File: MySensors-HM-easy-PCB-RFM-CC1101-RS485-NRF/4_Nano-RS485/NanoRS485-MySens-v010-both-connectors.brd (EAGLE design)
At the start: 25 x 35.5 mm, 47 parts, among them IC1 ATSHA204A, IC2 AT25DF512C-SSHN-B, IC3 REG1117, IC31 ATMEGA168-TQFP, X2 1751264, Y2 8MHZ

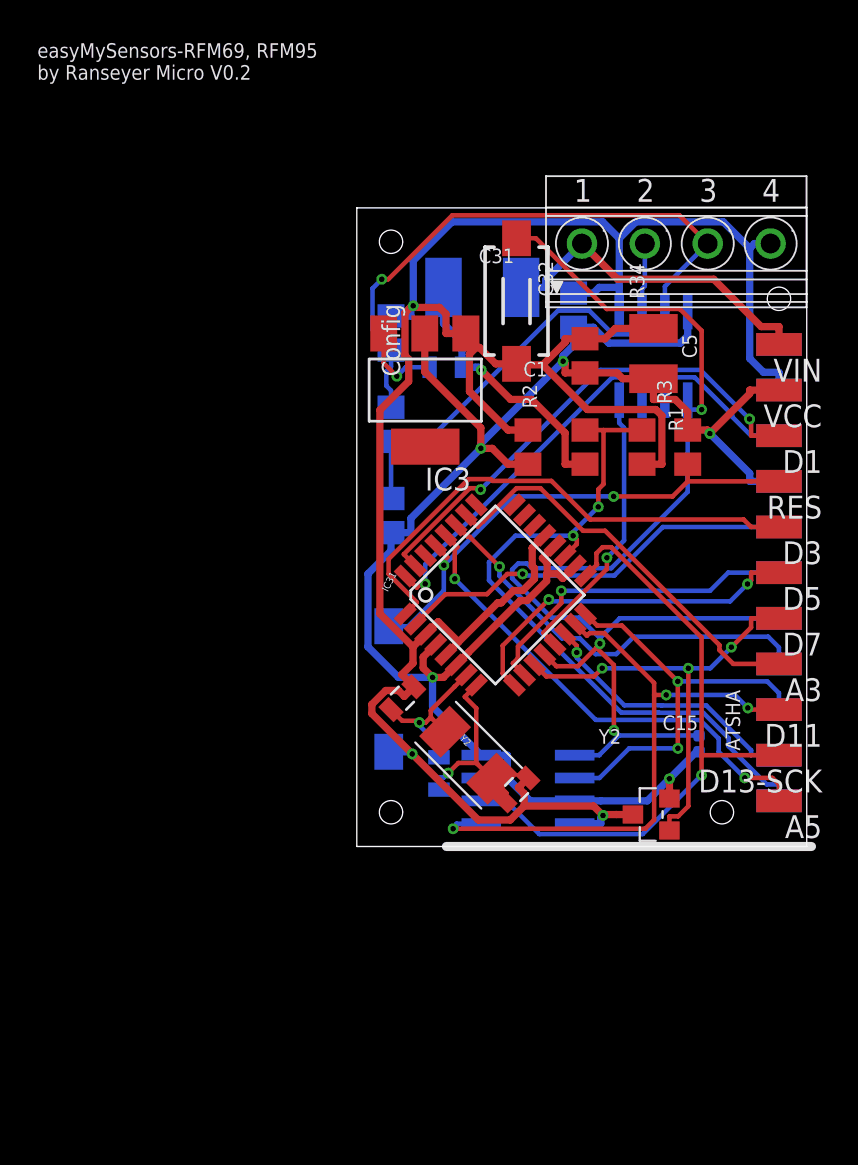
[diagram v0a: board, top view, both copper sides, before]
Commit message: RS485 New SubBoard
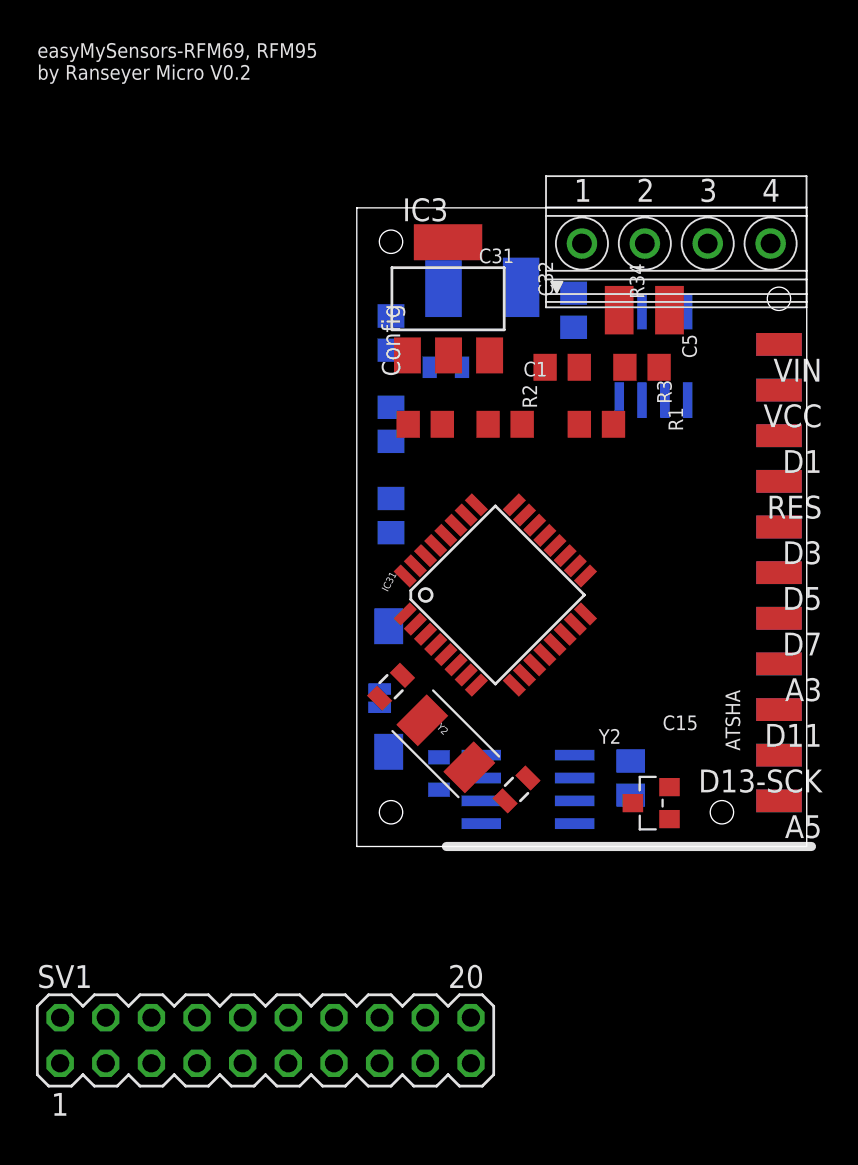
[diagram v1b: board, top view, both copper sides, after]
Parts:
- removed CONFIG: DTSM-3, mechanics:DTSM-3
- added JP1: JUMPER-SMT_2_NC_TRACE_SILK, SparkFun-Jumpers:SMT-JUMPER_2_NC_TRACE_SILK
- added SV1: (no value), con-lstb:MA10-2
- R2: device Discrete:R0402 -> resistor:M0805
- moved C32 5.85 mm to (3.81, 23.5), turned to 180 degrees
- moved IC3 5.24 mm to (5.08, 30.5), turned to 0 degrees
- moved R34 5.12 mm to (15.9, 26.7), turned to 0 degrees
- moved R1 4.62 mm to (8.26, 23.5), turned to 0 degrees
- moved R2 4.26 mm to (15.2, 3.81), turned to 270 degrees
- moved R3 2.84 mm to (13.3, 23.5), turned to 0 degrees
- moved C5 2.47 mm to (16.0, 29.8), turned to 180 degrees
- moved Y2 1.42 mm to (4.95, 5.71)
- moved C31 1.42 mm to (11.4, 26.7), turned to 180 degrees
- moved C14 0.90 mm to (1.91, 8.89)
- moved IC1 0.63 mm to (16.4, 2.41)
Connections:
- removed net 3V3: 3V3.1
- new net VCC1: IC2.3, IC2.7, IC2.8, JP1.1, R2.2
- net A0: now also SV1.8, VCC-LEGACY.1
- net A3: now also SV1.15
- net A4: now also SV1.16
- net D1-TXD: now also SV1.5
- net D10_SS: now also SV1.20
- net D11_MOSI: now also SV1.17
- net D12_MISO: now also SV1.18
- net D13_SCK: now also SV1.19
- net D2_INT0: no longer D2.1
- net D3: now also SV1.9
- net D4: now also SV1.10
- net D5: now also SV1.11
- net D6: now also SV1.12
- net D7-ATSHA: now also SV1.13
- net D8: now also SV1.14; no longer CONFIG.2
- net GND: now also SV1.4; no longer CONFIG.1
- net RESET: now also SV1.7
- net RXD: now also D2.1, SV1.6
- net VCC: now also 3V3.1, JP1.2, SV1.2, SV1.3; no longer IC2.3, IC2.7, IC2.8, R2.2, VCC-LEGACY.1
- net VIN: now also SV1.1
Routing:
- net GND: track 139.9 -> 0.00 mm, vias 3 -> 0
- net VCC: track 106.3 -> 0.00 mm, vias 5 -> 0
- net D8: track 68.6 -> 0.00 mm, vias 3 -> 0
- net A6: track 39.5 -> 0.00 mm, vias 2 -> 0
- net D13_SCK: track 36.0 -> 0.00 mm, vias 1 -> 0
- net D11_MOSI: track 33.9 -> 0.00 mm, vias 3 -> 0
- net B: track 33.5 -> 0.00 mm, vias 1 -> 0
- net D2_INT0: track 30.5 -> 0.00 mm, vias 1 -> 0
- net D3: track 28.6 -> 0.00 mm
- net RESET: track 28.3 -> 0.00 mm, vias 2 -> 0
- net D1-TXD: track 28.1 -> 0.00 mm, vias 2 -> 0
- net A5: track 26.9 -> 0.00 mm, vias 2 -> 0
- net A: track 25.9 -> 0.00 mm
- net D7-ATSHA: track 25.3 -> 0.00 mm, vias 3 -> 0
- net D12_MISO: track 23.7 -> 0.00 mm, vias 2 -> 0
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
